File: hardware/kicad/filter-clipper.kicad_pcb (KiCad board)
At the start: 2 copper layers, 140 x 90 mm, 23 parts, among them P401 JXF-FILT, P402 JFILT-WET, P403 JFILT-CTL-A, P404 JFILT-PWR, P405 JFILT-CTL-B, U401 OPA1679IDR, U402 OPA1679IDR

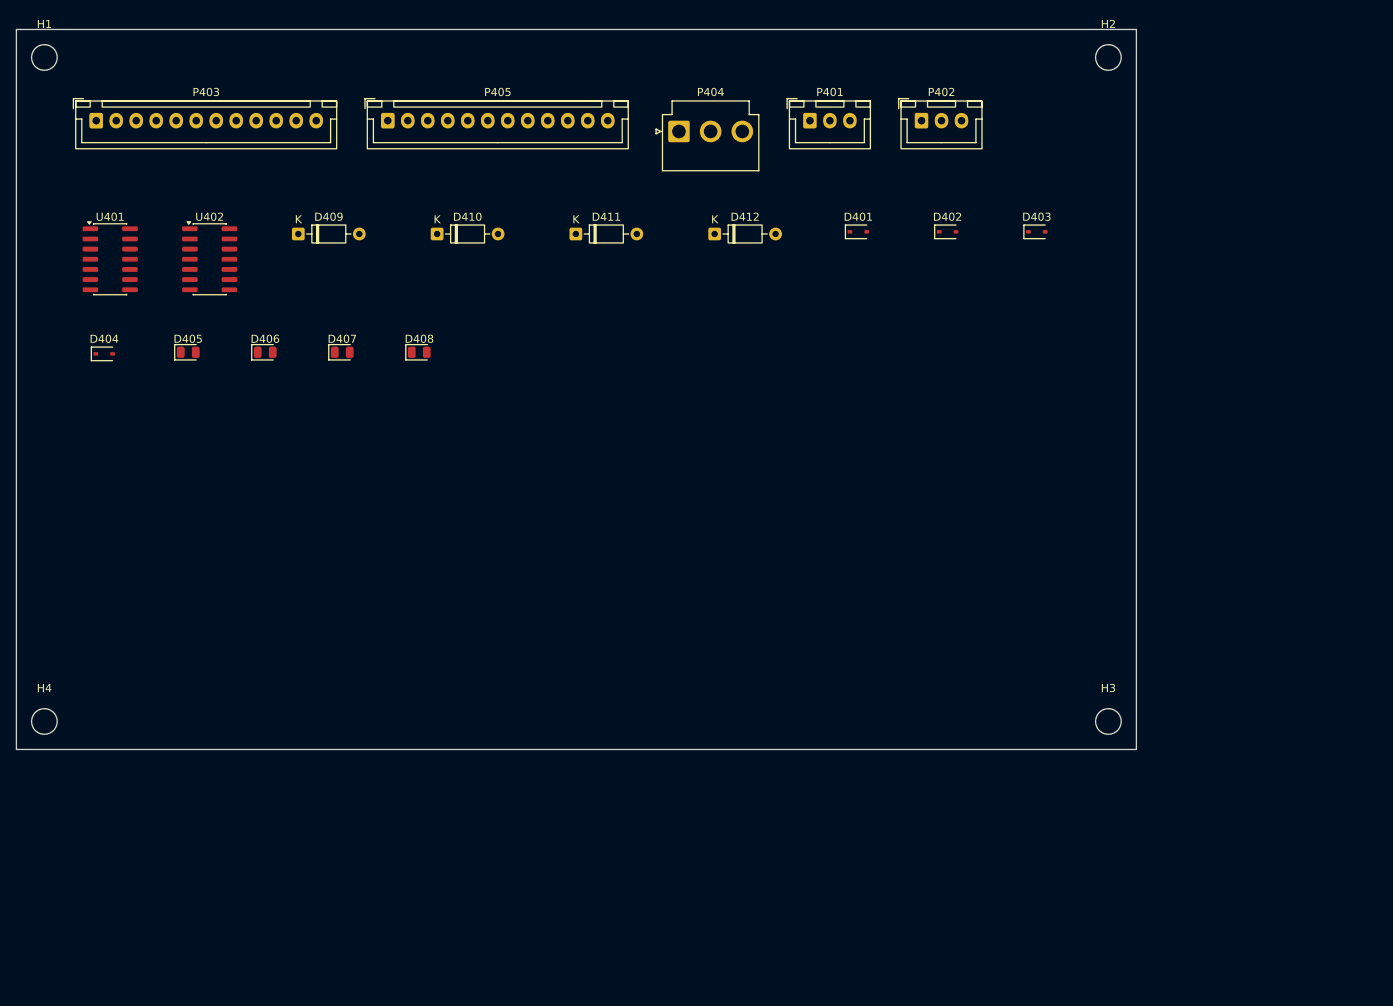
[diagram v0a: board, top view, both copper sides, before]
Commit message: Board 4 filter-clipper: ERC 0, sim verified (HPF/drive 4.9x/clip modes/LPF), routed DRC 0/0, fab outputs; clip decode = 3x G5V-2 relay tree per frozen truth table
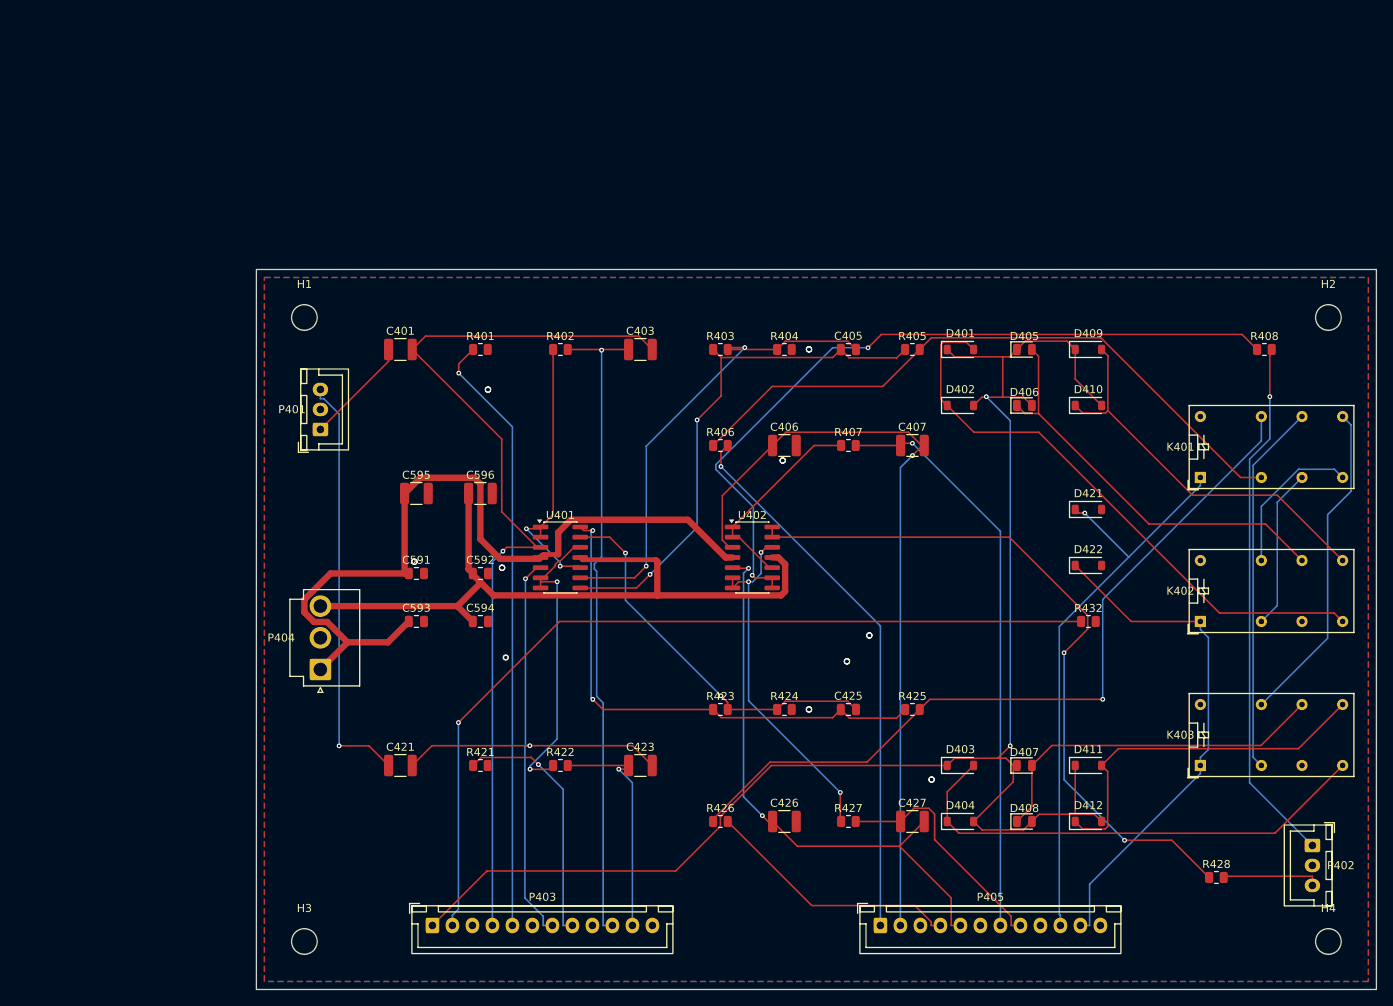
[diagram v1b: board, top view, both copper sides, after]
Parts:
- added C401: 47n, Capacitor_SMD:C_1210_3225Metric, F.Cu at (48.0, 40.0)
- added C403: 10n, Capacitor_SMD:C_1210_3225Metric, F.Cu at (78.0, 40.0)
- added C405: 47p, Capacitor_SMD:C_0805_2012Metric, F.Cu at (104.0, 40.0)
- added C406: 10n, Capacitor_SMD:C_1210_3225Metric, F.Cu at (96.0, 52.0)
- added C407: 10n, Capacitor_SMD:C_1210_3225Metric, F.Cu at (112.0, 52.0)
- added C421: 47n, Capacitor_SMD:C_1210_3225Metric, F.Cu at (48.0, 92.0)
- added C423: 10n, Capacitor_SMD:C_1210_3225Metric, F.Cu at (78.0, 92.0)
- added C425: 47p, Capacitor_SMD:C_0805_2012Metric, F.Cu at (104.0, 85.0)
- added C426: 10n, Capacitor_SMD:C_1210_3225Metric, F.Cu at (96.0, 99.0)
- added C427: 10n, Capacitor_SMD:C_1210_3225Metric, F.Cu at (112.0, 99.0)
- added C591: 100n, Capacitor_SMD:C_0805_2012Metric, F.Cu at (50.0, 68.0)
- added C592: 100n, Capacitor_SMD:C_0805_2012Metric, F.Cu at (58.0, 68.0)
- added C593: 100n, Capacitor_SMD:C_0805_2012Metric, F.Cu at (50.0, 74.0)
- added C594: 100n, Capacitor_SMD:C_0805_2012Metric, F.Cu at (58.0, 74.0)
- added C595: 22u, Capacitor_SMD:C_1210_3225Metric, F.Cu at (50.0, 58.0)
- added C596: 22u, Capacitor_SMD:C_1210_3225Metric, F.Cu at (58.0, 58.0)
- added D421: 1N4148W, Diode_SMD:D_SOD-123, F.Cu at (134.0, 60.0)
- added D422: 1N4148W, Diode_SMD:D_SOD-123, F.Cu at (134.0, 67.0)
- added K401: G5V-2 DC5, Relay_THT:Relay_DPDT_Omron_G5V-2, F.Cu at (148.0, 56.0)
- added K402: G5V-2 DC5, Relay_THT:Relay_DPDT_Omron_G5V-2, F.Cu at (148.0, 74.0)
- added K403: G5V-2 DC5, Relay_THT:Relay_DPDT_Omron_G5V-2, F.Cu at (148.0, 92.0)
- added R401: 1k, Resistor_SMD:R_0805_2012Metric, F.Cu at (58.0, 40.0)
- added R402: 47k, Resistor_SMD:R_0805_2012Metric, F.Cu at (68.0, 40.0)
- added R403: 39k, Resistor_SMD:R_0805_2012Metric, F.Cu at (88.0, 40.0)
- added R404: 10k, Resistor_SMD:R_0805_2012Metric, F.Cu at (96.0, 40.0)
- added R405: 4.7k, Resistor_SMD:R_0805_2012Metric, F.Cu at (112.0, 40.0)
- added R406: 1k, Resistor_SMD:R_0805_2012Metric, F.Cu at (88.0, 52.0)
- added R407: 47k, Resistor_SMD:R_0805_2012Metric, F.Cu at (104.0, 52.0)
- added R408: 100, Resistor_SMD:R_0805_2012Metric, F.Cu at (156.0, 40.0)
- added R421: 1k, Resistor_SMD:R_0805_2012Metric, F.Cu at (58.0, 92.0)
- added R422: 47k, Resistor_SMD:R_0805_2012Metric, F.Cu at (68.0, 92.0)
- added R423: 39k, Resistor_SMD:R_0805_2012Metric, F.Cu at (88.0, 85.0)
- added R424: 10k, Resistor_SMD:R_0805_2012Metric, F.Cu at (96.0, 85.0)
- added R425: 4.7k, Resistor_SMD:R_0805_2012Metric, F.Cu at (112.0, 85.0)
- added R426: 1k, Resistor_SMD:R_0805_2012Metric, F.Cu at (88.0, 99.0)
- added R427: 47k, Resistor_SMD:R_0805_2012Metric, F.Cu at (104.0, 99.0)
- added R428: 100, Resistor_SMD:R_0805_2012Metric, F.Cu at (150.0, 106.0)
- added R432: 100, Resistor_SMD:R_0805_2012Metric, F.Cu at (134.0, 74.0)
- D401, D402, D403, D404: value 1N4148WS -> 1N4148W; footprint D_SOD-323 -> Diode_SMD:D_SOD-123
- D405, D406, D407, D408: value Clip LED -> LED red; footprint LED_0805_2012Metric -> LED_SMD:LED_0805_2012Metric
- D409, D410, D411, D412: value Ge clip or adapter -> 1N5819HW; footprint D_DO-35_SOD27_P7.62mm_Horizontal -> Diode_SMD:D_SOD-123
- H1, H2, H3, H4: value M3 NPTH -> M3; footprint MountingHole_3.2mm_M3 -> MountingHole:MountingHole_3.2mm_M3
- P401: value JXF-FILT -> JXF-FILT B3B-XH-A; footprint JST_XH_B3B-XH-A_1x03_P2.50mm_Vertical -> Connector_JST:JST_XH_B3B-XH-A_1x03_P2.50mm_Vertical
- P402: value JFILT-WET -> JFILT-WET B3B-XH-A; footprint JST_XH_B3B-XH-A_1x03_P2.50mm_Vertical -> Connector_JST:JST_XH_B3B-XH-A_1x03_P2.50mm_Vertical
- P403: value JFILT-CTL-A -> JFILT-CTL-A B12B-XH-A; footprint JST_XH_B12B-XH-A_1x12_P2.50mm_Vertical -> Connector_JST:JST_XH_B12B-XH-A_1x12_P2.50mm_Vertical
- P404: value JFILT-PWR -> JFILT-PWR B3P-VH-B; footprint JST_VH_B3P-VH_1x03_P3.96mm_Vertical -> Connector_JST:JST_VH_B3P-VH_1x03_P3.96mm_Vertical
- P405: value JFILT-CTL-B -> JFILT-CTL-B B12B-XH-A; footprint JST_XH_B12B-XH-A_1x12_P2.50mm_Vertical -> Connector_JST:JST_XH_B12B-XH-A_1x12_P2.50mm_Vertical
- U401, U402: footprint SOIC-14_3.9x8.7mm_P1.27mm -> Package_SO:SOIC-14_3.9x8.7mm_P1.27mm
- moved H4 162.8 mm to (164.0, 114.0)
- moved D404 121.9 mm to (118.0, 99.0)
- moved P405 117.9 mm to (108.0, 112.0)
- moved P403 109.0 mm to (52.0, 112.0)
- moved D405 104.5 mm to (126.0, 40.0)
- moved H3 104.2 mm to (36.0, 114.0)
- moved P402 102.9 mm to (162.0, 102.0), turned to -90 degrees
- moved D409 99.8 mm to (134.0, 40.0)
- moved D407 99.7 mm to (126.0, 92.0)
- moved D408 95.7 mm to (126.0, 99.0)
- moved D406 95.1 mm to (126.0, 47.0)
- moved D411 92.3 mm to (134.0, 92.0)
- moved D412 87.0 mm to (134.0, 99.0)
- moved D410 84.2 mm to (134.0, 47.0)
- moved P404 80.8 mm to (38.0, 80.0), turned to 90 degrees
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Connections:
- D401 pad 1: (no net) -> DRV_HI
- D401 pad 2: (no net) -> N_SI_L
- D402 pad 1: (no net) -> N_SI_L
- D402 pad 2: (no net) -> DRV_HI
- D403 pad 1: (no net) -> DRV_HI
- D403 pad 2: (no net) -> N_SI_R
- D404 pad 1: (no net) -> N_SI_R
- D404 pad 2: (no net) -> DRV_HI
- D405 pad 1: (no net) -> DRV_HI
- D405 pad 2: (no net) -> N_LED_L
- D406 pad 1: (no net) -> N_LED_L
- D406 pad 2: (no net) -> DRV_HI
- D407 pad 1: (no net) -> DRV_HI
- D407 pad 2: (no net) -> N_LED_R
- D408 pad 1: (no net) -> N_LED_R
- D408 pad 2: (no net) -> DRV_HI
- D409 pad 1: (no net) -> DRV_HI
- D409 pad 2: (no net) -> N_GE_L
- D410 pad 1: (no net) -> N_GE_L
- D410 pad 2: (no net) -> DRV_HI
- D411 pad 1: (no net) -> DRV_HI
- D411 pad 2: (no net) -> N_GE_R
- D412 pad 1: (no net) -> N_GE_R
- D412 pad 2: (no net) -> DRV_HI
- P401 pad 1: (no net) -> XFADE_OUT_L
- P401 pad 2: (no net) -> AGND
- P401 pad 3: (no net) -> XFADE_OUT_R
- P402 pad 1: (no net) -> FILTCLIP_OUT_L
- P402 pad 2: (no net) -> AGND
- P402 pad 3: (no net) -> FILTCLIP_OUT_R
- P403 pad 1: (no net) -> DRV_HI
- P403 pad 10: (no net) -> HPF_Q_L_WIPER
- P403 pad 11: (no net) -> HPF_Q_R_WIPER
- P403 pad 12: (no net) -> AGND
- P403 pad 2: (no net) -> DRV_WIPER
- P403 pad 3: (no net) -> AGND
- P403 pad 4: (no net) -> HPF_F_L_HI
- P403 pad 5: (no net) -> HPF_F_L_WIPER
- P403 pad 6: (no net) -> AGND
- P403 pad 7: (no net) -> HPF_F_R_HI
- P403 pad 8: (no net) -> HPF_F_R_WIPER
- P403 pad 9: (no net) -> AGND
- P404 pad 1: (no net) -> +15VA
- P404 pad 2: (no net) -> AGND
- P404 pad 3: (no net) -> -15VA
- P405 pad 1: (no net) -> LPF_F_L_HI
- P405 pad 10: (no net) -> CTL_CLIP_MODE_A
- P405 pad 11: (no net) -> CTL_CLIP_MODE_B
- P405 pad 12: (no net) -> AGND
- P405 pad 2: (no net) -> LPF_F_L_WIPER
- P405 pad 3: (no net) -> AGND
- P405 pad 4: (no net) -> LPF_F_R_HI
- P405 pad 5: (no net) -> LPF_F_R_WIPER
- P405 pad 6: (no net) -> AGND
- P405 pad 7: (no net) -> LPF_Q_L_WIPER
- P405 pad 8: (no net) -> LPF_Q_R_WIPER
- P405 pad 9: (no net) -> +5VAUX
- U401 pad 1: (no net) -> N_HPF_OUT_L
- U401 pad 10: (no net) -> N_HPF_OUT_L
- U401 pad 11: (no net) -> -15VA
- U401 pad 12: (no net) -> N_HPF_OUT_R
- U401 pad 13: (no net) -> N_DRV_M_R
- U401 pad 14: (no net) -> N_DRV_OUT_R
- U401 pad 2: (no net) -> N_HPF_OUT_L
- U401 pad 3: (no net) -> HPF_F_L_HI
- U401 pad 4: (no net) -> +15VA
- U401 pad 5: (no net) -> HPF_F_R_HI
- U401 pad 6: (no net) -> N_HPF_OUT_R
- U401 pad 7: (no net) -> N_HPF_OUT_R
- U401 pad 8: (no net) -> N_DRV_OUT_L
- U401 pad 9: (no net) -> N_DRV_M_L
- U402 pad 1: (no net) -> N_LPF_OUT_L
- U402 pad 10: (no net) -> N_LPF_OUT_L
- U402 pad 11: (no net) -> -15VA
- U402 pad 12: (no net) -> N_LPF_OUT_R
- U402 pad 13: (no net) -> N_BUF_OUT_R
- U402 pad 14: (no net) -> N_BUF_OUT_R
- U402 pad 2: (no net) -> N_LPF_OUT_L
- U402 pad 3: (no net) -> LPF_F_L_WIPER
- U402 pad 4: (no net) -> +15VA
- U402 pad 5: (no net) -> LPF_F_R_WIPER
- U402 pad 6: (no net) -> N_LPF_OUT_R
- U402 pad 7: (no net) -> N_LPF_OUT_R
- U402 pad 8: (no net) -> N_BUF_OUT_L
- U402 pad 9: (no net) -> N_BUF_OUT_L
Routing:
- net DRV_HI: track 0.00 -> 201.9 mm, vias 0 -> 2
- net HPF_F_L_HI: track 0.00 -> 114.9 mm, vias 0 -> 1
- net DRV_WIPER: track 0.00 -> 108.7 mm, vias 0 -> 1
- net +15VA: track 0.00 -> 102.1 mm
- net N_CLIP_R: track 0.00 -> 98.8 mm, vias 0 -> 1
- net LPF_F_L_WIPER: track 0.00 -> 97.5 mm, vias 0 -> 1
- net N_BUF_OUT_L: track 0.00 -> 94.9 mm, vias 0 -> 2
- net -15VA: track 0.00 -> 94.1 mm
- net N_BUF_OUT_R: track 0.00 -> 89.7 mm, vias 0 -> 2
- net HPF_Q_L_WIPER: track 0.00 -> 81.6 mm, vias 0 -> 1
- net N_CLIP_L: track 0.00 -> 81.3 mm
- net HPF_F_R_HI: track 0.00 -> 80.5 mm, vias 0 -> 2
- net HPF_F_L_WIPER: track 0.00 -> 75.5 mm, vias 0 -> 1
- net N_SI_L: track 0.00 -> 73.2 mm
- net CTL_CLIP_MODE_A: track 0.00 -> 72.5 mm, vias 0 -> 1
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- added copper zone on B.Cu, net AGND
- added copper zone on F.Cu, net AGND
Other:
- board text removed: "GAS Rev A - Filter / Clipper Board"
- board text removed: "OUTLINE SCAFFOLD - NOT FOR FAB"
